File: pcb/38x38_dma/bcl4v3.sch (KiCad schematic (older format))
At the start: 33 parts, among them J1 Conn_01x04, J10 Conn_01x04, J2 Conn_01x04, J3 Conn_01x04, J4 Conn_01x04, J5 Conn_01x04, J6 Conn_01x04, J7 Conn_01x04, J8 Conn_01x04, J9 10118194-0001LF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

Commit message: Sync GPIO corrections, add tactile switch for BOOT0 signal
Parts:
- removed BOOT0: Jumper_2_Open, Jumpers:SMT-JUMPER_2_NO_SILK, symbol Jumper:Jumper_2_Open
- added BOOT0: B3U-1000P, digikey-footprints:Switch_Tactile_SMD_B3U-1000P, symbol dk_Tactile-Switches:B3U-1000P
- added C1: 22µF, Capacitor_Tantalum_SMD:CP_EIA-3528-15_AVX-H_Pad1.50x2.35mm_HandSolder, symbol Device:CP_Small
- LOGO1: symbol SparkFun-Aesthetics:OSHW-LOGOM -> bcl4v3-rescue:OSHW-LOGOM-SparkFun-Aesthetics
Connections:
- net labels added: SYN_RX, SYN_TX
- net labels removed: I2C_SCL, I2C_SDA
- wire segments 199 -> 207
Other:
- moved on the sheet: R2
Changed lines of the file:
@@
 	7250 2500 7750 2500
 Text Label 4500 3400 0    50   ~ 0
-I2C_SDA
+SYN_RX
 Text Label 4500 3500 0    50   ~ 0
-I2C_SCL
+SYN_TX
 $Comp
 L Connector_Generic:Conn_01x04 J1
@@
 	1200 2500 1050 2500
 Wire Wire Line
-	1200 2500 1200 2650
+	1200 2500 1200 2600
 Connection ~ 1200 2500
 Wire Wire Line
@@
 +5V
 Text Label 1300 1900 0    50   ~ 0
-I2C_SDA
+SYN_TX
 Text Label 1750 1900 0    50   ~ 0
-I2C_SDA
+SYN_RX
 Text Label 1300 2200 0    50   ~ 0
-I2C_SCL
+SYN_RX
 Text Label 1750 2200 0    50   ~ 0
-I2C_SCL
+SYN_TX
 Text Label 1300 3850 0    50   ~ 0
-I2C_SDA
+SYN_TX
 Text Label 1750 3850 0    50   ~ 0
-I2C_SDA
+SYN_RX
 Text Label 1300 4150 0    50   ~ 0
-I2C_SCL
+SYN_RX
 Text Label 1750 4150 0    50   ~ 0
-I2C_SCL
-$Comp
-L Transistor_FET:IRLML6402 Q1
-U 1 1 5BEBB389
-P 4200 6700
-F 0 "Q1" V 4543 6700 50  0000 C CNN
-F 1 "IRLML6402" V 4452 6700 50  0000 C CNN
-F 2 "Package_TO_SOT_SMD:SOT-23" H 4400 6625 50  0001 L CIN
-F 3 "https://www.infineon.com/dgdl/irlml6402pbf.pdf?fileId=5546d462533600a401535668d5c2263c" H 4200 6700 50  0001 L CNN
-	1    4200 6700
-	0    -1   -1   0
-$EndComp
+SYN_TX
 $Comp
 L power:GND #PWR0123
 U 1 1 5BEE0BDD
-P 4200 6900
-F 0 "#PWR0123" H 4200 6650 50  0001 C CNN
-F 1 "GND" H 4205 6727 50  0000 C CNN
-F 2 "" H 4200 6900 50  0001 C CNN
-F 3 "" H 4200 6900 50  0001 C CNN
-	1    4200 6900
+P 4200 7000
+F 0 "#PWR0123" H 4200 6750 50  0001 C CNN
+F 1 "GND" H 4205 6827 50  0000 C CNN
+F 2 "" H 4200 7000 50  0001 C CNN
+F 3 "" H 4200 7000 50  0001 C CNN
+	1    4200 7000
 	1    0    0    -1
 $EndComp
@@
 $EndComp
 Wire Wire Line
-	3800 1600 3850 1600
+	3800 1600 3900 1600
 Text Label 3950 1600 0    50   ~ 0
 BOOT0
@@
 L Device:R_Small R2
 U 1 1 5BF26B27
-P 3850 1800
-F 0 "R2" H 3909 1846 50  0000 L CNN
-F 1 "1k" H 3909 1755 50  0000 L CNN
-F 2 "Resistor_SMD:R_0805_2012Metric_Pad1.15x1.40mm_HandSolder" H 3850 1800 50  0001 C CNN
-F 3 "~" H 3850 1800 50  0001 C CNN
-	1    3850 1800
-	1    0    0    -1
-$EndComp
-Wire Wire Line
-	3850 1700 3850 1600
-Wire Wire Line
-	3850 1600 4200 1600
-Wire Wire Line
-	3850 1900 3850 2000
+P 3900 1800
+F 0 "R2" H 3959 1846 50  0000 L CNN
+F 1 "1k" H 3959 1755 50  0000 L CNN
+F 2 "Resistor_SMD:R_0805_2012Metric_Pad1.15x1.40mm_HandSolder" H 3900 1800 50  0001 C CNN
+F 3 "~" H 3900 1800 50  0001 C CNN
+	1    3900 1800
+	1    0    0    -1
+$EndComp
+Wire Wire Line
+	3900 1700 3900 1600
+Wire Wire Line
+	3900 1600 4200 1600
+Wire Wire Line
+	3900 1900 3900 2000
 $Comp
 L power:GND #PWR01
 U 1 1 5BF40857
-P 3850 2000
-F 0 "#PWR01" H 3850 1750 50  0001 C CNN
-F 1 "GND" H 3855 1827 50  0000 C CNN
-F 2 "" H 3850 2000 50  0001 C CNN
-F 3 "" H 3850 2000 50  0001 C CNN
-	1    3850 2000
-	1    0    0    -1
-$EndComp
-$Comp
-L Jumper:Jumper_2_Open BOOT0
-U 1 1 5BF40A5A
-P 3600 1600
-F 0 "BOOT0" H 3600 1750 50  0000 C CNN
-F 1 "Jumper_2_Open" H 3600 1744 50  0001 C CNN
-F 2 "Jumpers:SMT-JUMPER_2_NO_SILK" H 3600 1600 50  0001 C CNN
-F 3 "~" H 3600 1600 50  0001 C CNN
-	1    3600 1600
+P 3900 2000
+F 0 "#PWR01" H 3900 1750 50  0001 C CNN
+F 1 "GND" H 3905 1827 50  0000 C CNN
+F 2 "" H 3900 2000 50  0001 C CNN
+F 3 "" H 3900 2000 50  0001 C CNN
+	1    3900 2000
 	1    0    0    -1
 $EndComp
@@
 L power:+3.3V #PWR0116
 U 1 1 5BF4E4E1
-P 3300 1600
-F 0 "#PWR0116" H 3300 1450 50  0001 C CNN
-F 1 "+3.3V" H 3315 1773 50  0000 C CNN
-F 2 "" H 3300 1600 50  0001 C CNN
-F 3 "" H 3300 1600 50  0001 C CNN
-	1    3300 1600
+P 3300 1450
+F 0 "#PWR0116" H 3300 1300 50  0001 C CNN
+F 1 "+3.3V" H 3315 1623 50  0000 C CNN
+F 2 "" H 3300 1450 50  0001 C CNN
+F 3 "" H 3300 1450 50  0001 C CNN
+	1    3300 1450
 	1    0    0    -1
 $EndComp
@@
 Wire Notes Line style solid
 	550  7750 6900 7750
-Connection ~ 3850 1600
+Connection ~ 3900 1600
 Wire Notes Line style solid
 	550  4900 11100 4900
@@
 $EndComp
 $Comp
-L SparkFun-Aesthetics:OSHW-LOGOM LOGO1
+L bcl4v3-rescue:OSHW-LOGOM-SparkFun-Aesthetics LOGO1
 U 1 1 5BFECBD9
 P 3750 4450
@@
 Text Label 3600 3500 0    50   ~ 0
 CAT_DATA
+Wire Wire Line
+	3300 1600 3300 1450
+$Comp
+L dk_Tactile-Switches:B3U-1000P BOOT0
+U 1 1 5C14C2E1
+P 3600 1600
+F 0 "BOOT0" H 3600 1897 60  0000 C CNN
+F 1 "B3U-1000P" H 3600 1791 60  0000 C CNN
+F 2 "digikey-footprints:Switch_Tactile_SMD_B3U-1000P" H 3800 1800 60  0001 L CNN
+F 3 "https://omronfs.omron.com/en_US/ecb/products/pdf/en-b3u.pdf" H 3800 1900 60  0001 L CNN
+F 4 "SW1020CT-ND" H 3800 2000 60  0001 L CNN "Digi-Key_PN"
+F 5 "B3U-1000P" H 3800 2100 60  0001 L CNN "MPN"
+F 6 "Switches" H 3800 2200 60  0001 L CNN "Category"
+F 7 "Tactile Switches" H 3800 2300 60  0001 L CNN "Family"
+F 8 "https://omronfs.omron.com/en_US/ecb/products/pdf/en-b3u.pdf" H 3800 2400 60  0001 L CNN "DK_Datasheet_Link"
+F 9 "/product-detail/en/omron-electronics-inc-emc-div/B3U-1000P/SW1020CT-ND/1534357" H 3800 2500 60  0001 L CNN "DK_Detail_Page"
+F 10 "SWITCH TACTILE SPST-NO 0.05A 12V" H 3800 2600 60  0001 L CNN "Description"
+F 11 "Omron Electronics Inc-EMC Div" H 3800 2700 60  0001 L CNN "Manufacturer"
+F 12 "Active" H 3800 2800 60  0001 L CNN "Status"
+	1    3600 1600
+	1    0    0    -1
+$EndComp
+$Comp
+L Device:CP_Small C1
+U 1 1 5C14EFFD
+P 5900 7100
+F 0 "C1" H 5988 7146 50  0000 L CNN
+F 1 "22µF" H 5988 7055 50  0000 L CNN
+F 2 "Capacitor_Tantalum_SMD:CP_EIA-3528-15_AVX-H_Pad1.50x2.35mm_HandSolder" H 5900 7100 50  0001 C CNN
+F 3 "~" H 5900 7100 50  0001 C CNN
+	1    5900 7100
+	1    0    0    -1
+$EndComp
+$Comp
+L power:GND #PWR0131
+U 1 1 5C14F1BA
+P 5900 7250
+F 0 "#PWR0131" H 5900 7000 50  0001 C CNN
+F 1 "GND" H 5905 7077 50  0000 C CNN
+F 2 "" H 5900 7250 50  0001 C CNN
+F 3 "" H 5900 7250 50  0001 C CNN
+	1    5900 7250
+	1    0    0    -1
+$EndComp
+Wire Wire Line
+	5900 6950 5900 7000
+Wire Wire Line
+	5900 7200 5900 7250
+$Comp
+L power:VCC #PWR0130
+U 1 1 5C16B372
+P 5900 6950
+F 0 "#PWR0130" H 5900 6800 50  0001 C CNN
+F 1 "VCC" H 5917 7123 50  0000 C CNN
+F 2 "" H 5900 6950 50  0001 C CNN
+F 3 "" H 5900 6950 50  0001 C CNN
+	1    5900 6950
+	1    0    0    -1
+$EndComp
+$Comp
+L power:PWR_FLAG #FLG0101
+U 1 1 5C2D34FE
+P 1700 1300
+F 0 "#FLG0101" H 1700 1375 50  0001 C CNN
+F 1 "PWR_FLAG" H 1700 1474 50  0000 C CNN
+F 2 "" H 1700 1300 50  0001 C CNN
+F 3 "~" H 1700 1300 50  0001 C CNN
+	1    1700 1300
+	1    0    0    -1
+$EndComp
+Wire Wire Line
+	1700 1300 1250 1300
+Connection ~ 1250 1300
+$Comp
+L power:PWR_FLAG #FLG0102
+U 1 1 5C2E1A61
+P 4700 6500
+F 0 "#FLG0102" H 4700 6575 50  0001 C CNN
+F 1 "PWR_FLAG" H 4700 6674 50  0000 C CNN
+F 2 "" H 4700 6500 50  0001 C CNN
+F 3 "~" H 4700 6500 50  0001 C CNN
+	1    4700 6500
+	1    0    0    -1
+$EndComp
+Wire Wire Line
+	4700 6500 4700 6600
+$Comp
+L Transistor_FET:IRLML6402 Q1
+U 1 1 5BEBB389
+P 4200 6700
+F 0 "Q1" V 4543 6700 50  0000 C CNN
+F 1 "IRLML6402" V 4452 6700 50  0000 C CNN
+F 2 "Package_TO_SOT_SMD:SOT-23" H 4400 6625 50  0001 L CIN
+F 3 "https://www.infineon.com/dgdl/irlml6402pbf.pdf?fileId=5546d462533600a401535668d5c2263c" H 4200 6700 50  0001 L CNN
+	1    4200 6700
+	0    -1   -1   0
+$EndComp
+Wire Wire Line
+	4200 6900 4200 7000
+$Comp
+L power:PWR_FLAG #FLG0103
+U 1 1 5C354764
+P 1700 2600
+F 0 "#FLG0103" H 1700 2675 50  0001 C CNN
+F 1 "PWR_FLAG" H 1700 2774 50  0000 C CNN
+F 2 "" H 1700 2600 50  0001 C CNN
+F 3 "~" H 1700 2600 50  0001 C CNN
+	1    1700 2600
+	1    0    0    -1
+$EndComp
+Wire Wire Line
+	1700 2600 1200 2600
+Connection ~ 1200 2600
+Wire Wire Line
+	1200 2600 1200 2650
 $EndSCHEMATC

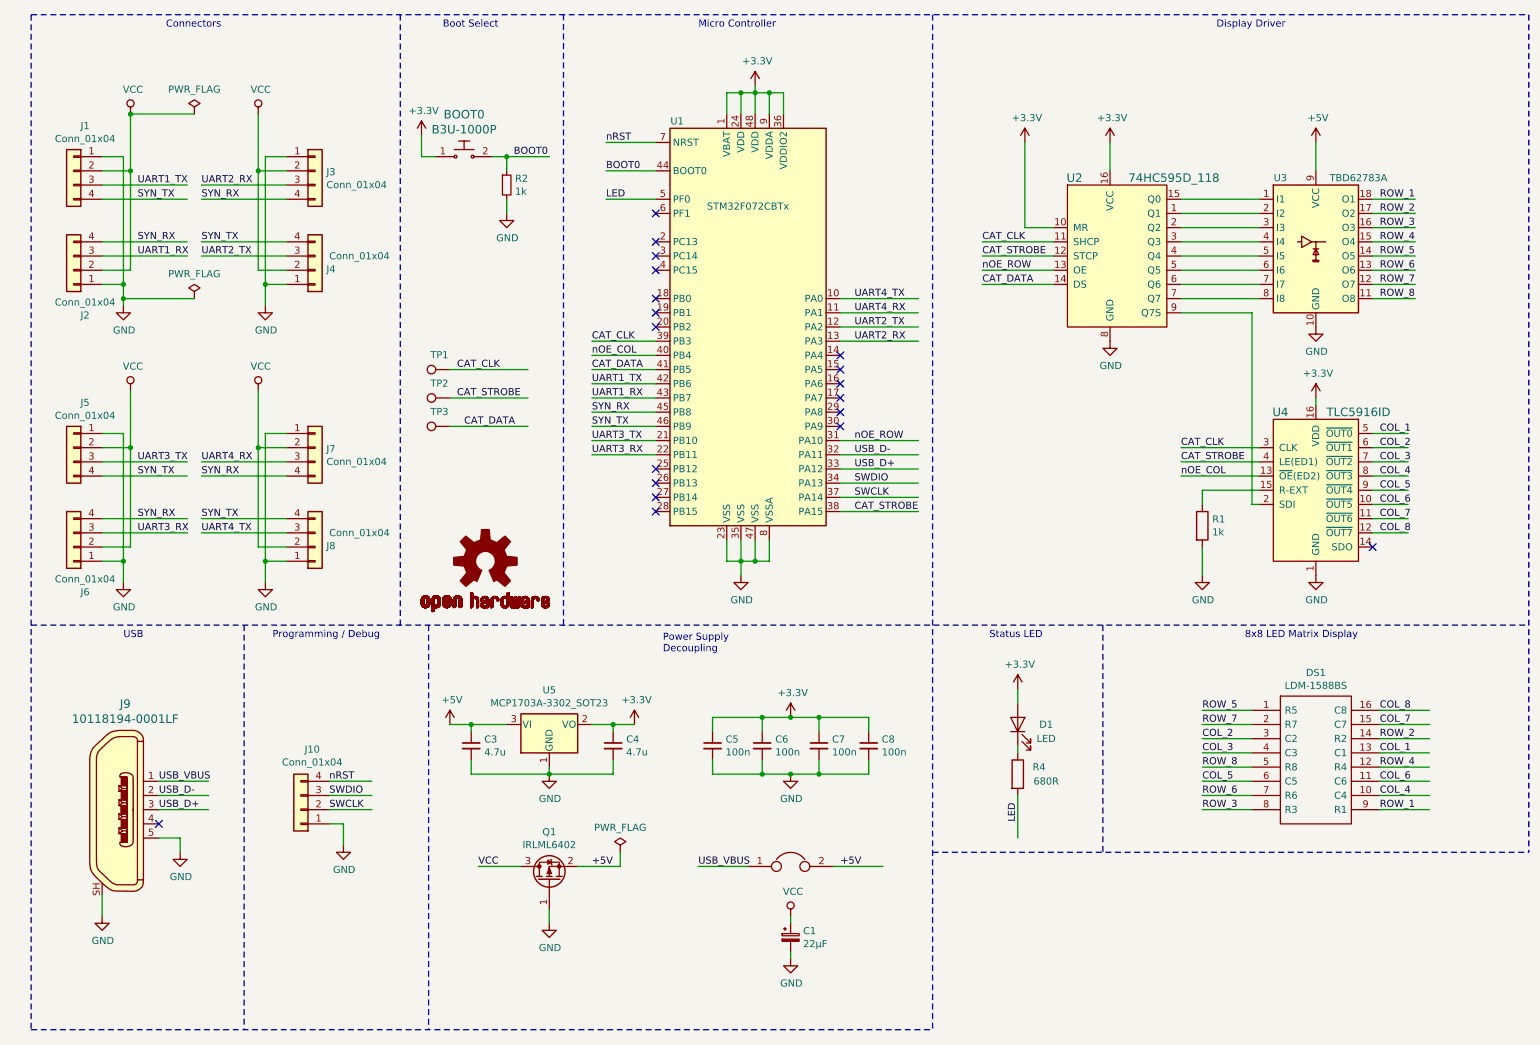
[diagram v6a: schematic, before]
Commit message: PCB updates: 32kHz oscillator, separate VBAT supply
also, longer pads for the row driver
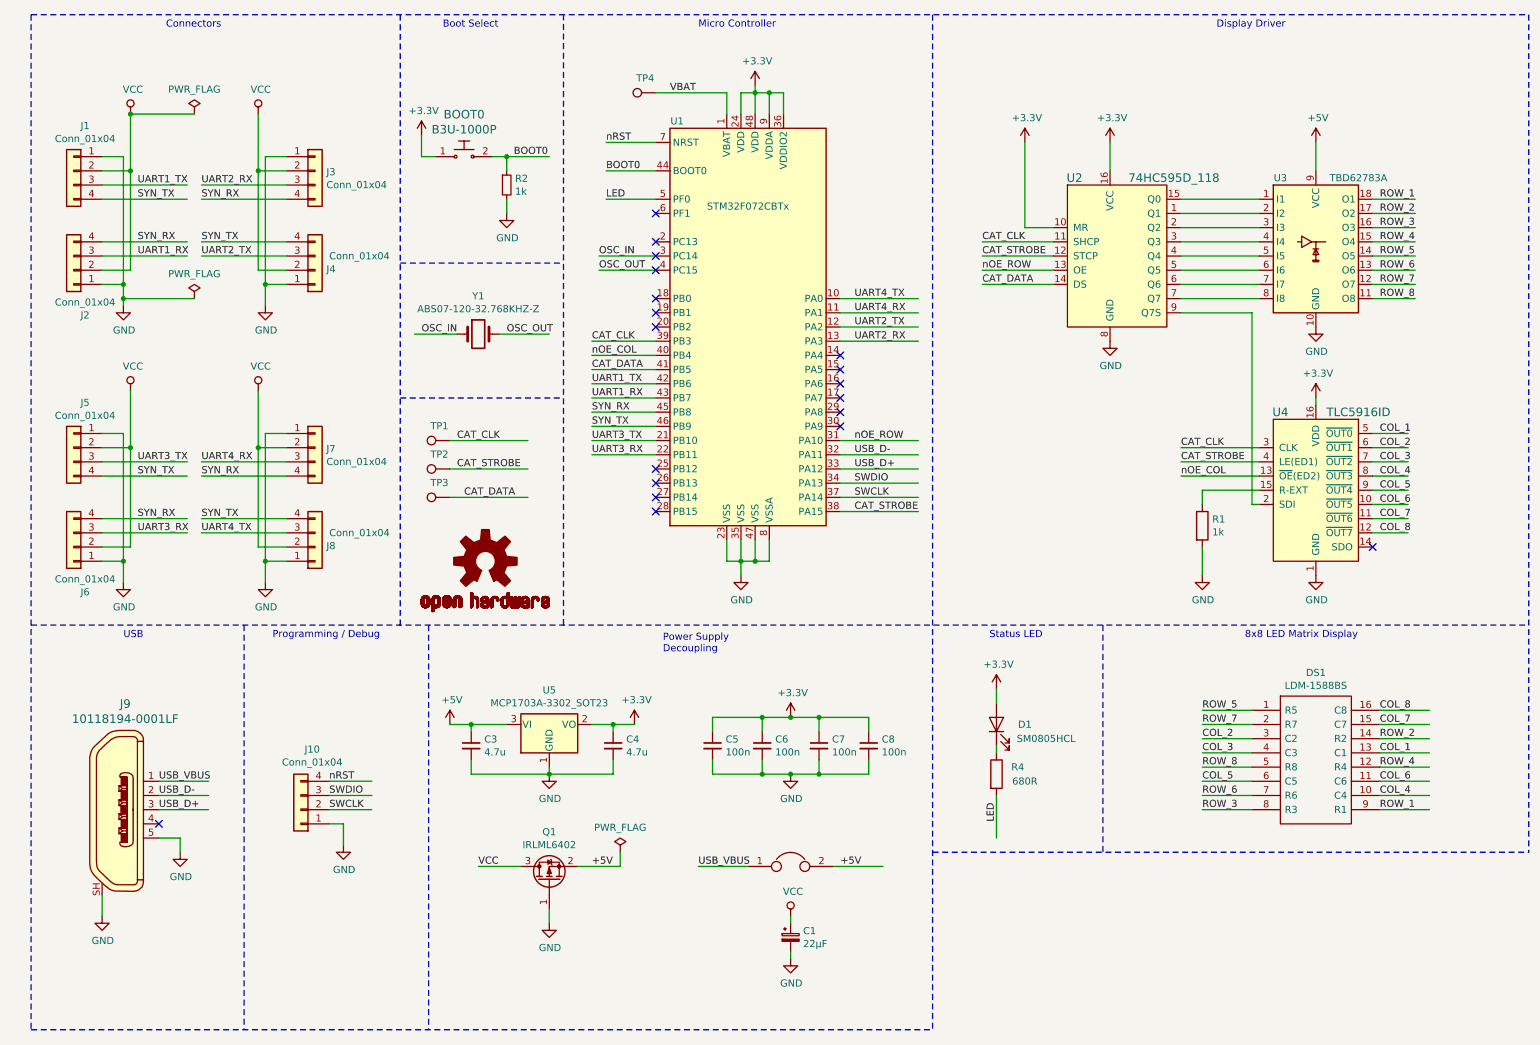
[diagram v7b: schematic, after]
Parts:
- added TP4: TestPoint, TestPoint:TestPoint_THTPad_1.0x1.0mm_Drill0.5mm, symbol Connector:TestPoint
- added Y1: ABS07-120-32.768KHZ-Z, Crystal:Crystal_SMD_MicroCrystal_CC7V-T1A-2Pin_3.2x1.5mm, symbol Device:Crystal
- D1: value LED -> SM0805HCL
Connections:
- net labels added: OSC_IN, OSC_OUT, VBAT
- wire segments 207 -> 211
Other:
- moved on the sheet: D1, R4, TP1, TP2, TP3
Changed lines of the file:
@@
 	5450 1300 5450 1150
 Wire Wire Line
-	5450 1150 5550 1150
-Wire Wire Line
 	5850 1150 5850 1300
 Wire Wire Line
 	5550 1300 5550 1150
-Connection ~ 5550 1150
 Wire Wire Line
 	5550 1150 5650 1150
@@
 L Device:LED D1
 U 1 1 5BF12B88
-P 7500 5600
-F 0 "D1" V 7500 5400 50  0000 C CNN
-F 1 "LED" V 7400 5400 50  0000 C CNN
-F 2 "LED_SMD:LED_0805_2012Metric_Castellated" H 7500 5600 50  0001 C CNN
-F 3 "~" H 7500 5600 50  0001 C CNN
-	1    7500 5600
+P 7350 5600
+F 0 "D1" V 7350 5400 50  0000 C CNN
+F 1 "SM0805HCL" V 7250 5250 50  0000 C CNN
+F 2 "LED_SMD:LED_0805_2012Metric_Castellated" H 7350 5600 50  0001 C CNN
+F 3 "~" H 7350 5600 50  0001 C CNN
+	1    7350 5600
 	0    -1   -1   0
 $EndComp
@@
 L Device:R R4
 U 1 1 5BF12DFF
-P 7500 5950
-F 0 "R4" H 7650 6000 50  0000 C CNN
-F 1 "680R" H 7700 5900 50  0000 C CNN
-F 2 "Resistor_SMD:R_0805_2012Metric_Pad1.15x1.40mm_HandSolder" V 7430 5950 50  0001 C CNN
-F 3 "~" H 7500 5950 50  0001 C CNN
-	1    7500 5950
-	1    0    0    -1
-$EndComp
-Wire Wire Line
-	7500 5750 7500 5800
-Wire Wire Line
-	7500 6100 7500 6400
-Wire Wire Line
-	7500 5450 7500 5350
+P 7350 5950
+F 0 "R4" H 7500 6000 50  0000 C CNN
+F 1 "680R" H 7550 5900 50  0000 C CNN
+F 2 "Resistor_SMD:R_0805_2012Metric_Pad1.15x1.40mm_HandSolder" V 7280 5950 50  0001 C CNN
+F 3 "~" H 7350 5950 50  0001 C CNN
+	1    7350 5950
+	1    0    0    -1
+$EndComp
+Wire Wire Line
+	7350 5750 7350 5800
+Wire Wire Line
+	7350 6100 7350 6400
+Wire Wire Line
+	7350 5450 7350 5350
 $Comp
 L power:+3.3V #PWR0124
 U 1 1 5BF45573
-P 7500 5350
-F 0 "#PWR0124" H 7500 5200 50  0001 C CNN
-F 1 "+3.3V" H 7515 5523 50  0000 C CNN
-F 2 "" H 7500 5350 50  0001 C CNN
-F 3 "" H 7500 5350 50  0001 C CNN
-	1    7500 5350
-	1    0    0    -1
-$EndComp
-Text Label 7500 6150 3    50   ~ 0
+P 7350 5350
+F 0 "#PWR0124" H 7350 5200 50  0001 C CNN
+F 1 "+3.3V" H 7365 5523 50  0000 C CNN
+F 2 "" H 7350 5350 50  0001 C CNN
+F 3 "" H 7350 5350 50  0001 C CNN
+	1    7350 5350
+	1    0    0    -1
+$EndComp
+Text Label 7350 6150 3    50   ~ 0
 LED
 $Comp
@@
 L Connector:TestPoint TP1
 U 1 1 5C01787F
-P 3500 3100
-F 0 "TP1" V 3603 3174 50  0000 C CNN
-F 1 "TestPoint" V 3604 3174 50  0001 C CNN
-F 2 "TestPoint:TestPoint_THTPad_1.0x1.0mm_Drill0.5mm" H 3700 3100 50  0001 C CNN
-F 3 "~" H 3700 3100 50  0001 C CNN
-	1    3500 3100
+P 3500 3600
+F 0 "TP1" V 3603 3674 50  0000 C CNN
+F 1 "TestPoint" V 3604 3674 50  0001 C CNN
+F 2 "TestPoint:TestPoint_THTPad_1.0x1.0mm_Drill0.5mm" H 3700 3600 50  0001 C CNN
+F 3 "~" H 3700 3600 50  0001 C CNN
+	1    3500 3600
 	0    -1   -1   0
 $EndComp
@@
 L Connector:TestPoint TP2
 U 1 1 5C03F55A
-P 3500 3300
-F 0 "TP2" V 3603 3374 50  0000 C CNN
-F 1 "TestPoint" V 3604 3374 50  0001 C CNN
-F 2 "TestPoint:TestPoint_THTPad_1.0x1.0mm_Drill0.5mm" H 3700 3300 50  0001 C CNN
-F 3 "~" H 3700 3300 50  0001 C CNN
-	1    3500 3300
+P 3500 3800
+F 0 "TP2" V 3603 3874 50  0000 C CNN
+F 1 "TestPoint" V 3604 3874 50  0001 C CNN
+F 2 "TestPoint:TestPoint_THTPad_1.0x1.0mm_Drill0.5mm" H 3700 3800 50  0001 C CNN
+F 3 "~" H 3700 3800 50  0001 C CNN
+	1    3500 3800
 	0    -1   -1   0
 $EndComp
@@
 L Connector:TestPoint TP3
 U 1 1 5C03F5B8
-P 3500 3500
-F 0 "TP3" V 3603 3574 50  0000 C CNN
-F 1 "TestPoint" V 3604 3574 50  0001 C CNN
-F 2 "TestPoint:TestPoint_THTPad_1.0x1.0mm_Drill0.5mm" H 3700 3500 50  0001 C CNN
-F 3 "~" H 3700 3500 50  0001 C CNN
-	1    3500 3500
+P 3500 4000
+F 0 "TP3" V 3603 4074 50  0000 C CNN
+F 1 "TestPoint" V 3604 4074 50  0001 C CNN
+F 2 "TestPoint:TestPoint_THTPad_1.0x1.0mm_Drill0.5mm" H 3700 4000 50  0001 C CNN
+F 3 "~" H 3700 4000 50  0001 C CNN
+	1    3500 4000
 	0    -1   -1   0
 $EndComp
 Wire Wire Line
-	3500 3100 4050 3100
-Wire Wire Line
-	3500 3300 4050 3300
-Wire Wire Line
-	3500 3500 4050 3500
-Text Label 3550 3100 0    50   ~ 0
+	3500 3600 4050 3600
+Wire Wire Line
+	3500 3800 4050 3800
+Wire Wire Line
+	3500 4000 4050 4000
+Text Label 3550 3600 0    50   ~ 0
 CAT_CLK
-Text Label 3550 3300 0    50   ~ 0
+Text Label 3550 3800 0    50   ~ 0
 CAT_STROBE
-Text Label 3600 3500 0    50   ~ 0
+Text Label 3600 4000 0    50   ~ 0
 CAT_DATA
 Wire Wire Line
@@
 Wire Wire Line
 	1200 2600 1200 2650
+Wire Wire Line
+	4550 2300 4950 2300
+Wire Wire Line
+	4550 2400 4950 2400
+Text Label 4550 2300 0    50   ~ 0
+OSC_IN
+Text Label 4550 2400 0    50   ~ 0
+OSC_OUT
+Wire Notes Line
+	3150 3300 4300 3300
+Wire Notes Line
+	3150 2350 4300 2350
+$Comp
+L Device:Crystal Y1
+U 1 1 5C5D348B
+P 3700 2850
+F 0 "Y1" H 3700 3118 50  0000 C CNN
+F 1 "ABS07-120-32.768KHZ-Z" H 3700 3027 50  0000 C CNN
+F 2 "Crystal:Crystal_SMD_MicroCrystal_CC7V-T1A-2Pin_3.2x1.5mm" H 3700 2850 50  0001 C CNN
+F 3 "~" H 3700 2850 50  0001 C CNN
+	1    3700 2850
+	1    0    0    -1
+$EndComp
+Wire Wire Line
+	3250 2850 3550 2850
+Wire Wire Line
+	4200 2850 3850 2850
+Text Label 3300 2850 0    50   ~ 0
+OSC_IN
+Text Label 3900 2850 0    50   ~ 0
+OSC_OUT
+$Comp
+L Connector:TestPoint TP4
+U 1 1 5C6B3B4E
+P 4950 1150
+F 0 "TP4" V 5053 1224 50  0000 C CNN
+F 1 "TestPoint" V 5054 1224 50  0001 C CNN
+F 2 "TestPoint:TestPoint_THTPad_1.0x1.0mm_Drill0.5mm" H 5150 1150 50  0001 C CNN
+F 3 "~" H 5150 1150 50  0001 C CNN
+	1    4950 1150
+	0    -1   -1   0
+$EndComp
+Wire Wire Line
+	5450 1150 4950 1150
+Text Label 5050 1150 0    50   ~ 0
+VBAT
 $EndSCHEMATC
